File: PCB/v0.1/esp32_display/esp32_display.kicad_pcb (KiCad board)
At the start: 2 copper layers, 91.4 x 71.1 mm, 36 parts, among them J1 USB_B_Micro, J2 Conn_01x06_Male, SW1 RST_BTN, SW2 SCREEN_OFF_BTN, U1 ESP32-WROOM-32, U2 MAX1821, U3 Display_ILI9341

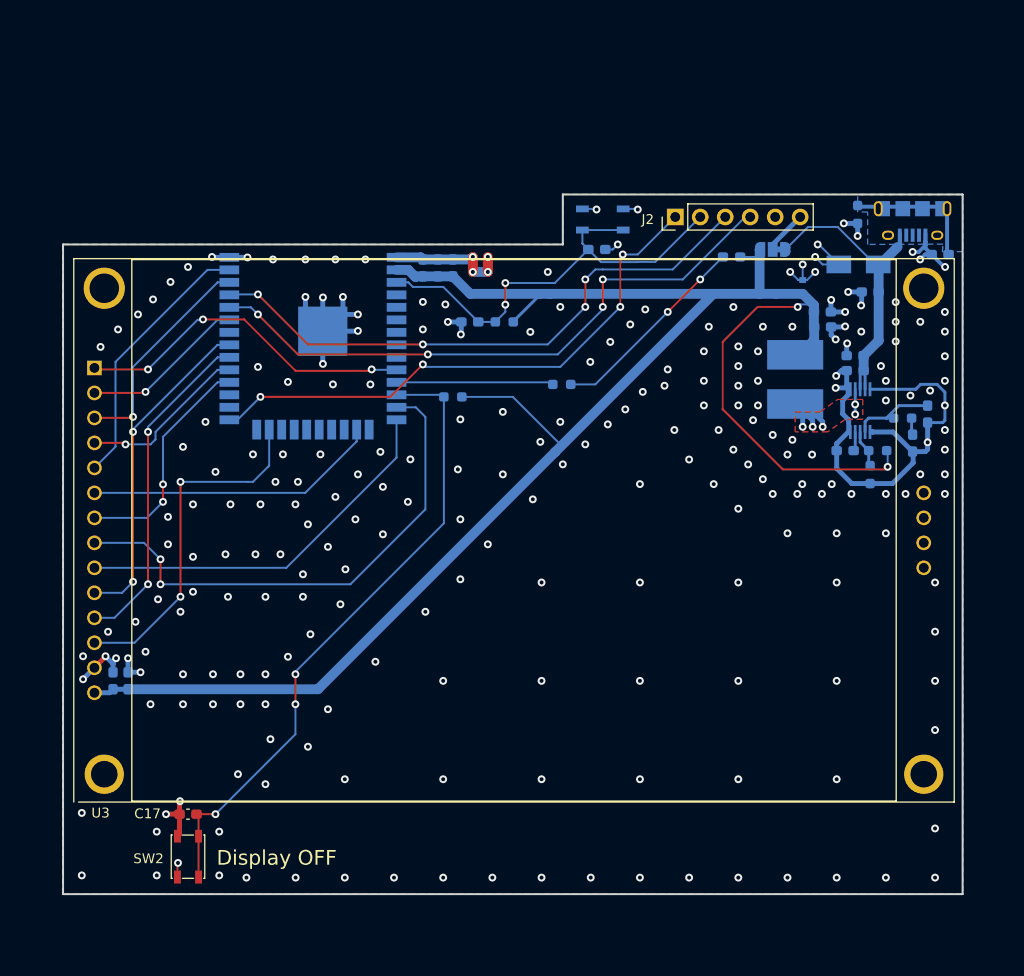
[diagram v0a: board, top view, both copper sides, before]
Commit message: Add housing edge, generate output files
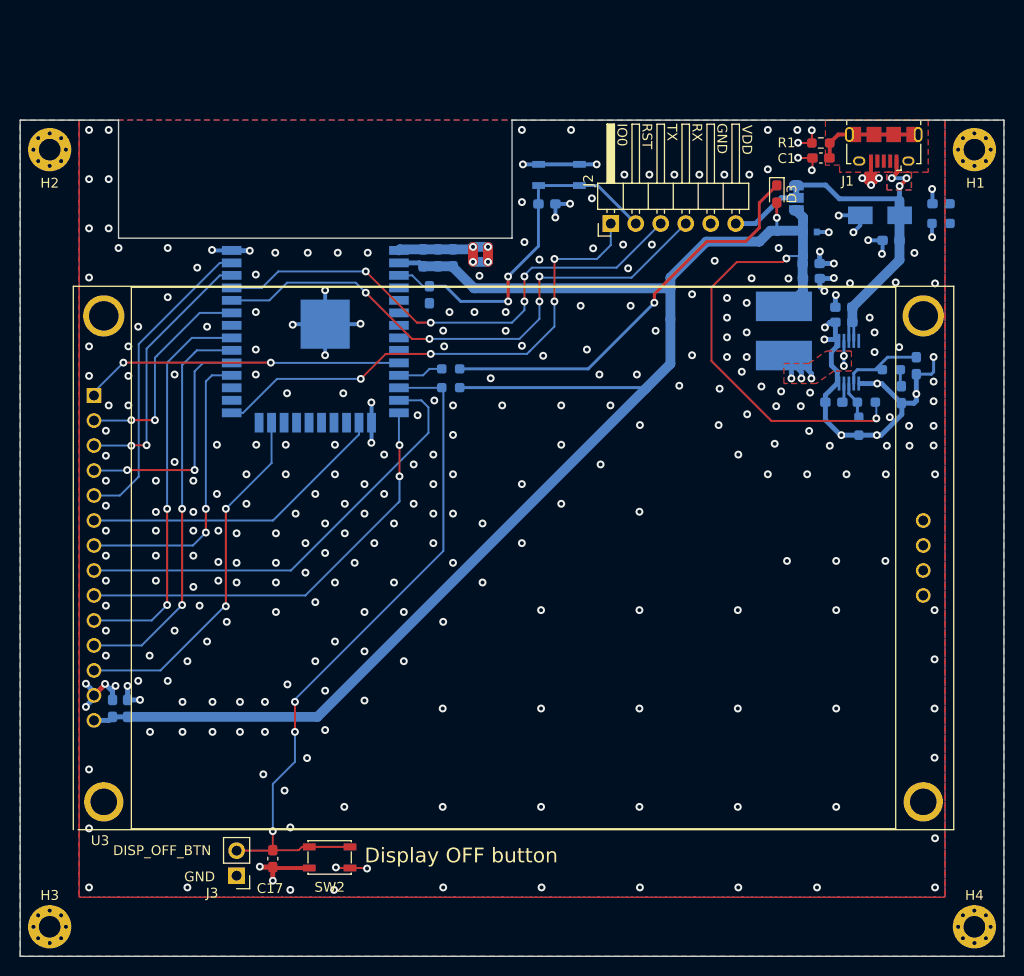
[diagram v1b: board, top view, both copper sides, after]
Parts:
- removed R4: 51k, Resistor_SMD:R_0603_1608Metric_Pad0.98x0.95mm_HandSolder
- added ?: , clipboard:7993e13b-3ecd-4363-bb88-0d37e634a5af, B.Cu at (93.9, 56.4)
- added C18: 4.7nF, Capacitor_SMD:C_0603_1608Metric_Pad1.08x0.95mm_HandSolder, B.Cu at (175.6, 36.5)
- added G***: LOGO, myLib:tabaluga_10x10, B.Cu at (166.8, 101.6)
- added H1: MountingHole_Pad, MountingHole:MountingHole_2.2mm_M2_Pad_Via, F.Cu at (179.0, 31.0)
- added H2: MountingHole_Pad, MountingHole:MountingHole_2.2mm_M2_Pad_Via, F.Cu at (85.0, 31.0)
- added H3: MountingHole_Pad, MountingHole:MountingHole_2.2mm_M2_Pad_Via, F.Cu at (85.0, 110.0)
- added H4: MountingHole_Pad, MountingHole:MountingHole_2.2mm_M2_Pad_Via, F.Cu at (179.0, 110.0)
- added J3: External button, Connector_PinHeader_2.54mm:PinHeader_1x02_P2.54mm_Vertical, F.Cu at (104.0, 104.8)
- added R8: 1M, Resistor_SMD:R_0603_1608Metric_Pad0.98x0.95mm_HandSolder, B.Cu at (175.6, 38.5)
- C1, D3, J1, R1: moved to F.Cu
- J2: footprint Connector_PinHeader_2.54mm:PinHeader_1x06_P2.54mm_Vertical -> Connector_PinHeader_2.54mm:PinHeader_1x06_P2.54mm_Horizontal
- moved C1 15.6 mm to (163.4, 31.9)
- moved SW2 14.4 mm to (113.5, 103.0), turned to 0 degrees
- moved R2 11.4 mm to (125.8, 53.3)
- moved C17 9.74 mm to (107.7, 103.1), turned to -90 degrees
- moved R1 8.17 mm to (163.4, 30.3), turned to 180 degrees
- moved J1 8.09 mm to (169.8, 30.8), turned to 180 degrees
- moved D3 7.88 mm to (158.9, 35.5), turned to -90 degrees
- moved C16 6.86 mm to (135.5, 36.5)
- moved J2 6.59 mm to (142.0, 38.5)
- moved SW1 6.35 mm to (136.8, 33.6)
- moved JP1 5.77 mm to (160.9, 35.9), turned to -90 degrees
- moved C2 5.65 mm to (170.5, 40.2)
- moved D2 5.63 mm to (162.3, 39.4), turned to 0 degrees
- moved D1 5.45 mm to (169.4, 37.7)
- moved L1 5.05 mm to (159.6, 49.4)
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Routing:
- net Net-(D3-Pad1): track 20.8 -> 42.0 mm, vias 2 -> 1
- net /MCU/LED_STATUS: track 16.0 -> 4.63 mm
- net /MCU/RST: track 45.9 -> 36.8 mm
- net +3V3: track 191.1 -> 199.1 mm, vias 2 -> 3
- net /MCU/DISP.DC: track 33.2 -> 40.3 mm
- net /MCU/DISP.SPI_CLK: track 52.8 -> 45.7 mm, vias 2 -> 0
- net /MCU/TOUCH.SPI_CS: track 17.4 -> 24.4 mm, vias 1 -> 2
- net /MCU/DISP.BCKL: track 23.3 -> 30.2 mm
- net /MCU/UART_TX: track 59.5 -> 52.7 mm
- net /MCU/DISP.RST: track 34.1 -> 40.7 mm
- net /MCU/UART_RX: track 62.5 -> 56.8 mm
- net /MCU/TOUCH.SPI_MISO: track 16.8 -> 22.3 mm, vias 1 -> 2
- net /MCU/IO0: track 57.1 -> 51.8 mm
- net /MCU/DISP.SPI_MISO: track 39.2 -> 44.0 mm, vias 0 -> 2
- net /MCU/SCREEN_OFF_BTN: track 65.5 -> 70.3 mm
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- added copper zone on B.Cu, net +5V
- added copper zone on F.Cu, net +5V
- added copper zone on B.Cu, net /HOUSING
- added copper zone on F.Cu, net /HOUSING
- added copper zone on F.Cu, net Net-(C1-Pad1)
- removed copper zone on B.Cu, net Net-(C1-Pad1)
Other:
- board size 91.4 x 71.1 mm -> 100 x 85 mm
- board text added: "3.3V"
- board text added: "5V"
- board text added: "Bzgec"
- board text added: "DISP_OFF_BTN"
- board text added: "D_BCKL"
- board text added: "D_CLK"
- board text added: "D_CS"
- board text added: "D_DC"
- board text added: "D_MISO"
- board text added: "D_RST"
- board text added: "Display OFF button"
- board text added: "Display_MQTT v0.1"
- board text added: "GND"
- board text added: "IO0"
- board text added: "RST"
- board text added: "RX"
- board text added: "Reset"
- board text added: "TX"
- board text added: "VDD"
- board text removed: "Display OFF"

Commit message: Smaller footprint, no housing, right angle buttons
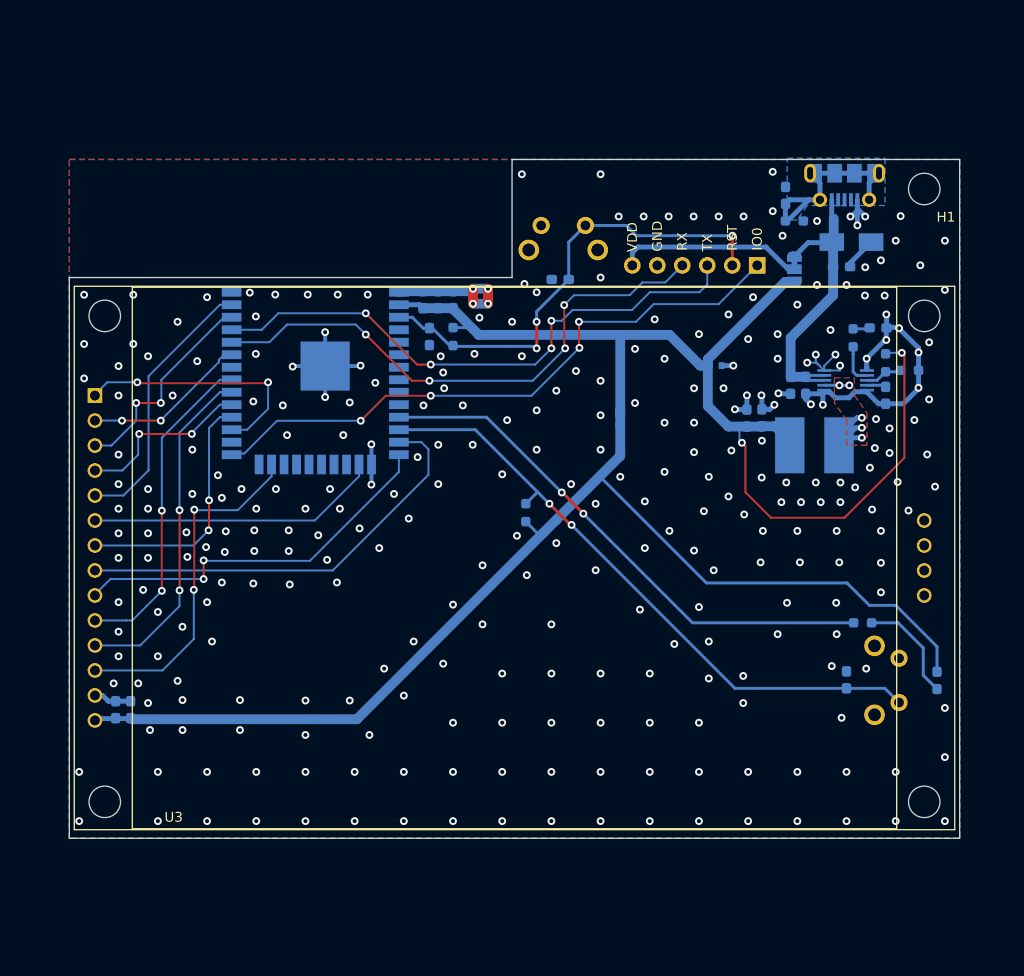
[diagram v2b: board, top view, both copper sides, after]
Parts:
- removed ?: , clipboard:7993e13b-3ecd-4363-bb88-0d37e634a5af
- removed C12: 0.1pF, Capacitor_SMD:C_0603_1608Metric_Pad1.08x0.95mm_HandSolder
- removed C18: 4.7nF, Capacitor_SMD:C_0603_1608Metric_Pad1.08x0.95mm_HandSolder
- removed H2, H3, H4: MountingHole_Pad, MountingHole:MountingHole_2.2mm_M2_Pad_Via
- removed J3: External button, Connector_PinHeader_2.54mm:PinHeader_1x02_P2.54mm_Vertical
- removed R8: 1M, Resistor_SMD:R_0603_1608Metric_Pad0.98x0.95mm_HandSolder
- added R4: 51k, Resistor_SMD:R_0603_1608Metric_Pad0.98x0.95mm_HandSolder, B.Cu at (126.0, 50.0)
- C1, C17, D3, J2, R1: moved to B.Cu
- C9: value 0.047uF -> 47nF
- H1: footprint MountingHole:MountingHole_2.2mm_M2_Pad_Via -> MountingHole:MountingHole_3.2mm_M3_ISO14580
- J1: footprint Connector_USB:USB_Micro-B_Amphenol_10118194_Horizontal -> Connector_USB:USB_Micro-B_Molex-105017-0001; moved to B.Cu
- SW1: footprint myLib:SW_SPST_PTS810 -> Button_Switch_THT:SW_Tactile_SPST_Angled_PTS645Vx83-2LFS
- SW2: footprint myLib:SW_SPST_PTS810 -> Button_Switch_THT:SW_Tactile_SPST_Angled_PTS645Vx83-2LFS; moved to B.Cu
- moved C17 61.1 mm to (166.0, 84.9), turned to 90 degrees
- moved SW2 60.0 mm to (171.3, 87.2), turned to 90 degrees
- moved D3 52.1 mm to (175.2, 85.0), turned to 90 degrees
- moved R2 49.2 mm to (167.6, 79.1)
- moved G*** 20.9 mm to (148.9, 90.8)
- moved C13 17.0 mm to (155.9, 58.3), turned to 90 degrees
- moved D2 16.7 mm to (152.6, 53.0)
- moved J2 15.5 mm to (156.9, 42.8)
- moved C11 15.0 mm to (157.4, 58.3), turned to 90 degrees
- moved R3 14.8 mm to (133.4, 67.9), turned to 90 degrees
- moved L1 12.0 mm to (162.7, 61.1), turned to 180 degrees
- moved C7 9.61 mm to (160.3, 55.0), turned to -90 degrees
- moved R1 8.37 mm to (160.7, 38.3), turned to 0 degrees
- moved C16 7.80 mm to (136.9, 44.2), turned to 180 degrees
- moved R7 7.67 mm to (172.4, 53.4), turned to 0 degrees
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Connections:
- net /MCU/SCREEN_OFF_BTN renamed /MCU/SCRN_OFF_BTN
- U1 pad 10: /MCU/TOUCH.IRQ -> unconnected-(U1-Pad10)
- U1 pad 27: unconnected-(U1-Pad27) -> /MCU/TOUCH.IRQ
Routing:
- net /MCU/LED_STATUS: track 4.63 -> 54.9 mm, vias 0 -> 2
- net GND: track 136.3 -> 89.9 mm, vias 315 -> 300
- net Net-(D3-Pad1): track 42.0 -> 11.1 mm, vias 1 -> 0
- net +3V3: track 199.1 -> 226.0 mm, vias 3 -> 2
- net Net-(J2-Pad6): track 7.25 -> 18.9 mm
- net /MCU/RST: track 36.8 -> 48.3 mm, vias 2 -> 3
- net /MCU/IO0: track 51.8 -> 63.0 mm
- net Net-(C1-Pad1): track 10.9 -> 21.9 mm
- net /MCU/DISP.DC: track 40.3 -> 33.3 mm
- net /MCU/TOUCH.IRQ: track 32.6 -> 25.6 mm
- net /MCU/TOUCH.SPI_CS: track 24.4 -> 18.1 mm
- net /MCU/SCRN_OFF_BTN: track 70.3 -> 64.0 mm, vias 3 -> 2
- net +5V: track 35.7 -> 29.9 mm, vias 3 -> 0
- net /MCU/DISP.RST: track 40.7 -> 35.0 mm
- net /MCU/UART_TX: track 52.7 -> 58.1 mm
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- added copper zone on B.Cu, net Net-(C1-Pad1)
- removed copper zone on B.Cu, net +5V
- removed copper zone on F.Cu, net +5V
- removed copper zone on B.Cu, net /HOUSING
- removed copper zone on F.Cu, net /HOUSING
- removed copper zone on F.Cu, net Net-(C1-Pad1)
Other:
- board size 100 x 85 mm -> 90.5 x 69 mm
- board text added: "D_MOSI"
- board text added: "ESP32_display v0.1"
- board text added: "T_CLK"
- board text added: "T_CS"
- board text added: "T_IRQ"
- board text added: "T_MISO"
- board text added: "T_MOSI"
- board text removed: "Display OFF button"
- board text removed: "Display_MQTT v0.1"

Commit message: Add serial resistors to SPI lines (PCB not finished)
Still missing placment of RC filters.
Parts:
- removed C16, C17: 4.7nF, Capacitor_SMD:C_0603_1608Metric_Pad1.08x0.95mm_HandSolder
- added C6: 0.1uF, Capacitor_SMD:C_0603_1608Metric_Pad1.08x0.95mm_HandSolder, F.Cu at (129.6, 24.2)
- added R10: 30, Resistor_SMD:R_0603_1608Metric_Pad0.98x0.95mm_HandSolder, B.Cu at (107.6, 66.8)
- added R11: 30, Resistor_SMD:R_0603_1608Metric_Pad0.98x0.95mm_HandSolder, B.Cu at (99.9, 54.4)
- added R12: 30, Resistor_SMD:R_0603_1608Metric_Pad0.98x0.95mm_HandSolder, B.Cu at (99.9, 48.3)
- added R13: 30, Resistor_SMD:R_0603_1608Metric_Pad0.98x0.95mm_HandSolder, B.Cu at (99.9, 46.6)
- added R14: 220, Resistor_SMD:R_0603_1608Metric_Pad0.98x0.95mm_HandSolder, B.Cu at (149.3, 46.3)
- added R15: 220, Resistor_SMD:R_0603_1608Metric_Pad0.98x0.95mm_HandSolder, B.Cu at (151.8, 46.3)
- added R16: 220, Resistor_SMD:R_0603_1608Metric_Pad0.98x0.95mm_HandSolder, B.Cu at (154.4, 46.3)
- added R17: 220, Resistor_SMD:R_0603_1608Metric_Pad0.98x0.95mm_HandSolder, B.Cu at (156.9, 46.3)
- added R21: 30, Resistor_SMD:R_0603_1608Metric_Pad0.98x0.95mm_HandSolder, B.Cu at (92.9, 56.0)
- added R22: 30, Resistor_SMD:R_0603_1608Metric_Pad0.98x0.95mm_HandSolder, B.Cu at (92.9, 58.5)
- added R23: 30, Resistor_SMD:R_0603_1608Metric_Pad0.98x0.95mm_HandSolder, B.Cu at (92.9, 76.3)
- added R4: 1k, Resistor_SMD:R_0603_1608Metric_Pad0.98x0.95mm_HandSolder, F.Cu at (129.6, 21.6)
- added R6: 1k, Resistor_SMD:R_0603_1608Metric_Pad0.98x0.95mm_HandSolder, F.Cu at (108.4, 20.3)
- added R7: 30, Resistor_SMD:R_0603_1608Metric_Pad0.98x0.95mm_HandSolder, B.Cu at (99.9, 56.9)
- added R8: 30, Resistor_SMD:R_0603_1608Metric_Pad0.98x0.95mm_HandSolder, B.Cu at (116.4, 66.8)
- added R9: 30, Resistor_SMD:R_0603_1608Metric_Pad0.98x0.95mm_HandSolder, B.Cu at (124.1, 60.7)
- renumbered C9 to C10, C10 to C11, C11 to C12, C6 to C7, C7 to C8, C8 to C9, R5 to R18, R6 to R19, R7 to R20, R4 to R5
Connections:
- C7 pad 1: /MCU/RST -> Net-(C7-Pad1)
- J2 pad 1: /MCU/IO0 -> Net-(J2-Pad1)
- J2 pad 2: /MCU/RST -> Net-(J2-Pad2)
- J2 pad 3: /MCU/UART_TX -> Net-(J2-Pad3)
- J2 pad 4: /MCU/UART_RX -> Net-(J2-Pad4)
- R3 pad 2: /MCU/SCRN_OFF_BTN -> Net-(R3-Pad2)
- SW2 pad 1: /MCU/SCRN_OFF_BTN -> Net-(R3-Pad2)
- U1 pad 13: /MCU/DISP.SPI_CLK -> Net-(R9-Pad1)
- U1 pad 16: /MCU/DISP.SPI_MOSI -> Net-(R8-Pad1)
- U1 pad 23: /MCU/DISP.SPI_CS -> Net-(R10-Pad1)
- U1 pad 29: /MCU/TOUCH.SPI_CS -> Net-(R7-Pad1)
- U1 pad 3: /MCU/RST -> Net-(C7-Pad1)
- U1 pad 31: /MCU/DISP.DC -> Net-(R11-Pad1)
- U1 pad 36: /MCU/TOUCH.SPI_MOSI -> Net-(R12-Pad1)
- U1 pad 37: /MCU/TOUCH.SPI_CLK -> Net-(R13-Pad1)
- U3 pad 1: /MCU/TOUCH.IRQ -> Net-(R21-Pad1)
- U3 pad 2: /MCU/TOUCH.SPI_MISO -> Net-(R22-Pad1)
- U3 pad 9: /MCU/DISP.SPI_MISO -> Net-(R23-Pad1)
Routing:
- net Net-(R3-Pad2): track 0.00 -> 64.0 mm, vias 0 -> 2
- net /MCU/SCRN_OFF_BTN: track 64.0 -> 0.00 mm, vias 2 -> 0
- net /MCU/RST: track 48.3 -> 0.00 mm, vias 3 -> 0
- net Net-(C7-Pad1): track 0.00 -> 28.6 mm, vias 0 -> 2
- net +3V3: track 226.0 -> 212.1 mm
- net /MCU/TOUCH.IRQ: track 25.6 -> 21.2 mm
- net /MCU/TOUCH.SPI_CS: track 18.1 -> 15.0 mm
- net Net-(R13-Pad1): track 0.00 -> 2.87 mm
- net Net-(R12-Pad1): track 0.00 -> 2.87 mm
- net Net-(R8-Pad1): track 0.00 -> 2.83 mm
- net Net-(R10-Pad1): track 0.00 -> 2.83 mm
- net /MCU/DISP.SPI_MOSI: track 30.0 -> 27.3 mm
- net Net-(R9-Pad1): track 0.00 -> 2.70 mm
- net Net-(R7-Pad1): track 0.00 -> 2.70 mm
- net Net-(R11-Pad1): track 0.00 -> 2.70 mm
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
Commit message: Rename TVS/ESD protection diodes to their name (5V and 3.3V)
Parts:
- D1: value D_Zener - 5.0V -> SMAJ5.0CA
- D2: value D_Zener - 3.3V -> ESD5Z3.3T1G
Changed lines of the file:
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@@
       (effects (font (size 1 1) (thickness 0.15)) (justify mirror))
     )
-    (fp_text value "D_Zener - 5.0V" (at 0 -2.6) (layer "B.Fab")
+    (fp_text value "SMAJ5.0CA" (at 0 -2.6) (layer "B.Fab")
       (effects (font (size 1 1) (thickness 0.15)) (justify mirror))
     )
@@
       (effects (font (size 1 1) (thickness 0.15)) (justify mirror))
     )
-    (fp_text value "D_Zener - 3.3V" (at 0 -1.4) (layer "B.Fab")
-      (effects (font (size 1 1) (thickness 0.15)) (justify mirror))
-    )
+    (fp_text value "ESD5Z3.3T1G" (at 0 -1.4) (layer "B.Fab")
+      (effects (font (size 1 1) (thickness 0.15)) (justify mirror))
+    )
